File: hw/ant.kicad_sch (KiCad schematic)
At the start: 3 parts, among them J701 Conn_Coaxial_Power, K701 G5Q-1

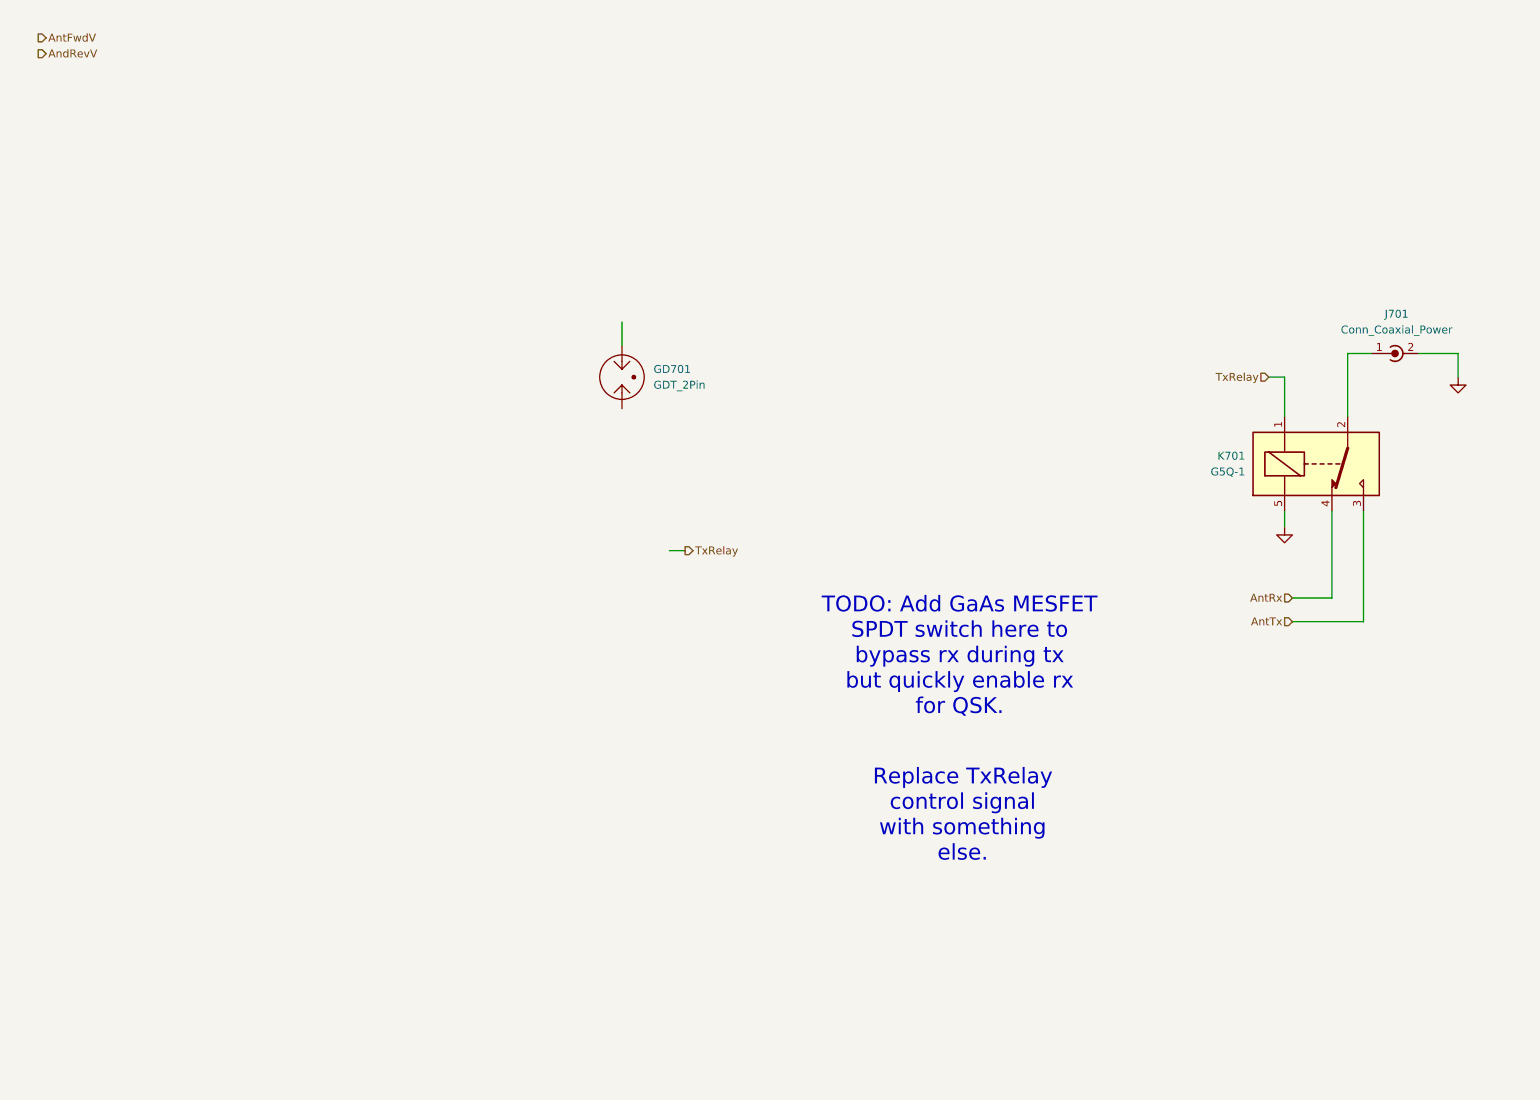
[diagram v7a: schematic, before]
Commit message: Moved ant page into tx page, added Bruene Direction Coupler to measure VSWR. General cleanup, page renumber, reannote
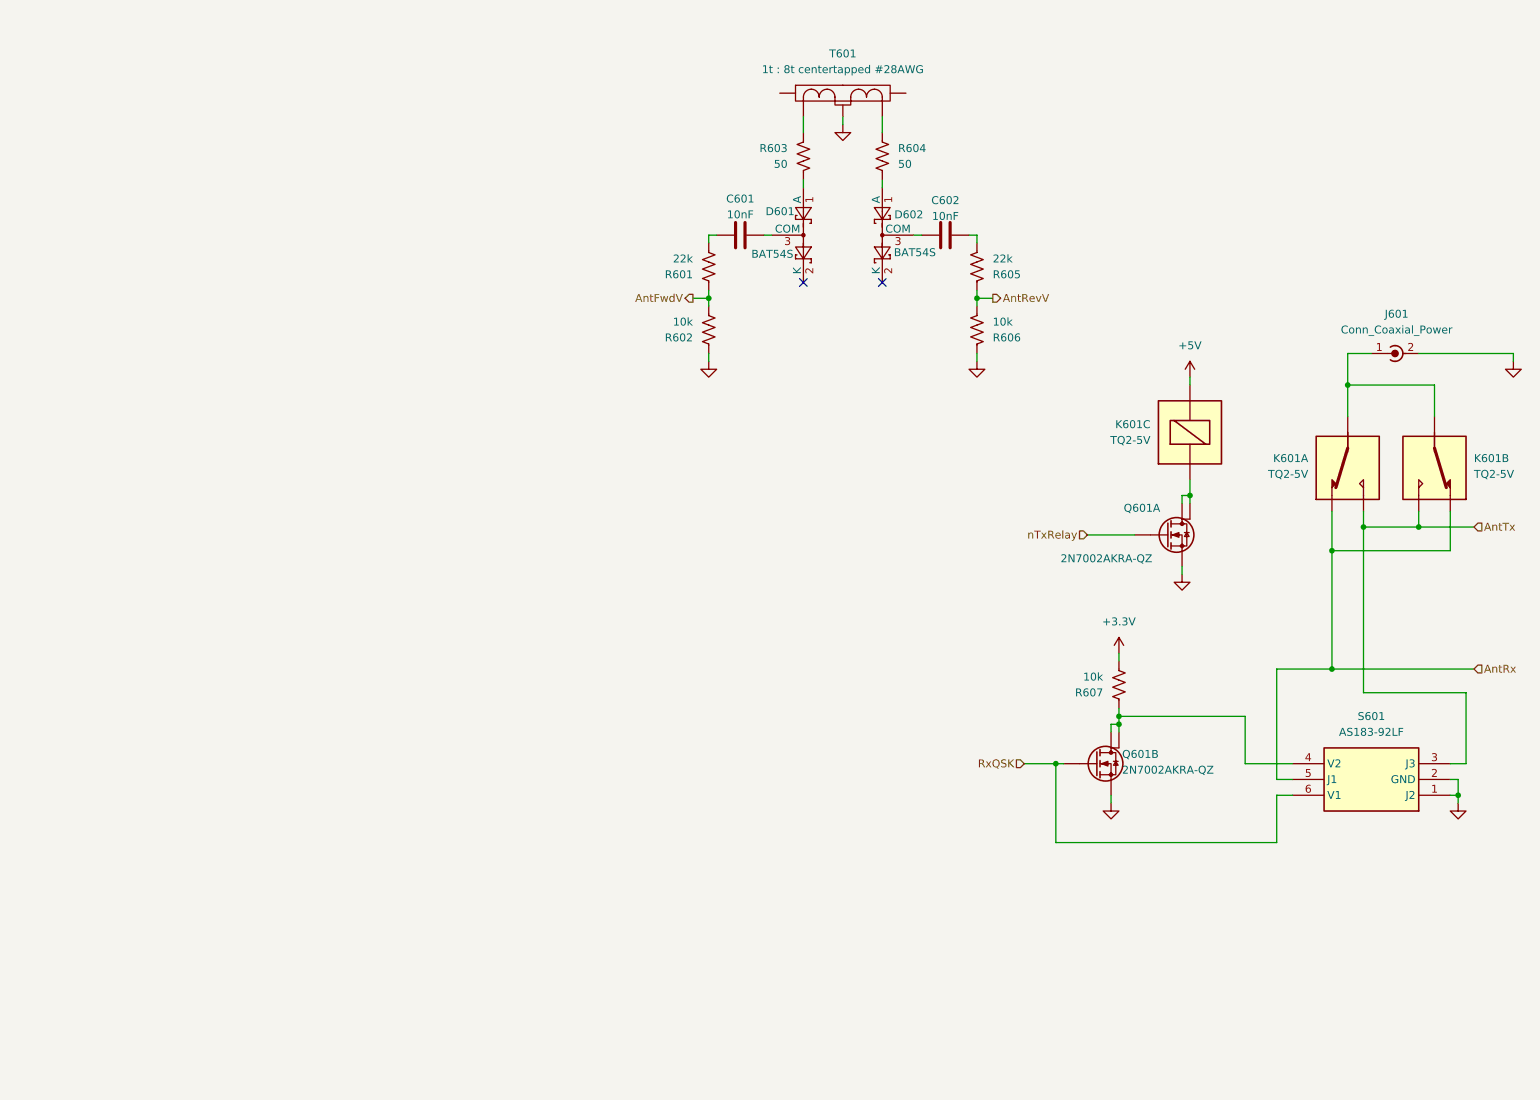
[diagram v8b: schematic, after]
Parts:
- removed GD701: GDT_2Pin, symbol Device:GDT_2Pin
- removed K701: G5Q-1, Relay_THT:Relay_SPDT_Omron-G5Q-1, symbol Relay:G5Q-1
- added C601, C602: 10nF, symbol Device:C
- added D601, D602: BAT54S, Package_TO_SOT_SMD:SOT-23, symbol Diode:BAT54S
- added K601: TQ2-5V, symbol Library:TQ2-5V
- added Q601: 2N7002AKRA-QZ, 2N7002AKRAQZ, symbol 2N7002AKRA-QZ:2N7002AKRA-QZ
- added R601, R605: 22k, symbol Device:R_US
- added R602, R606, R607: 10k, symbol Device:R_US
- added R603, R604: 50, symbol Device:R_US
- added S601: AS183-92LF, SOT65P220X110-6N, symbol AS183-92LF:AS183-92LF
- added T601: 1t : 8t centertapped #28AWG, symbol Library:Tandem_Coupler
- renumbered J701 to J601
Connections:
- net AntFwdV: now also R601.1, R602.2
- net AntRx: now also K601.5 (NC1), K601.6, K601.6 (T2), K601.8 (NC2), S601.5 (J1)
- net AntTx: now also K601.4 (NO1), K601.9, K601.9, S601.3 (J3)
- net GND: now also Q601.1 (S1), Q601.4 (S2), R602.1, R606.1, S601.1 (J2), S601.2 (GND), T601.3
- net at J601.1 (In): now also K601.16, K601.16, K601.3 (T1), K601.4, K601.4 (NO1), K601.6 (T2)
- new net: Q601.3 (D2_1), Q601.8 (D2_2), R607.1, S601.4 (V2)
- new net: D601.1 (A), R603.2
- new net: C601.2, D601.3 (COM)
- new net: D602.1 (A), R604.2
- new net: C602.2, D602.3 (COM)
- new net: K601.9 (C1), Q601.6 (D1), Q601.7 (D2)
- new net: C602.1, R605.2
- new net: C601.1, R601.2
- new net: R603.1, T601.5
- new net: R604.1, T601.4
- new net +3.3V: R607.2
- new net +5V: K601.10 (C2)
- new net AntRevV: R605.1, R606.2
- new net RxQSK: Q601.5 (G2), S601.6 (V1)
- new net nTxRelay: Q601.2 (G1)
- no-connect marks 0 -> 2
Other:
- note removed: "Replace TxRelay control signal with something else."
- note removed: "TODO: Add GaAs MESFET SPDT switch here to bypass rx during tx but quickly enable rx for QSK."
